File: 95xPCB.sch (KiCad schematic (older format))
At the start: 20 parts

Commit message: v1b2.7
more matrix stuff
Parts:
- removed R? (x2): 22, symbol Device:R_Small
- added R? (x2): R_Small, symbol Device:R_Small
- gave numbers to parts that had none: 18
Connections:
- net labels added: col0, col1, col10, col11, col12, col13, col14, col2, col3, col4, col7, col8, col9
- wire segments 84 -> 95
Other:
- moved on the sheet: J1

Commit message: v1b3
who knows at this point, let's be real it was kicad doing a funny
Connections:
- wire segments 95 -> 90
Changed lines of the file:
@@
 col14
 Wire Wire Line
-	4500 4000 4850 4000
-Wire Wire Line
-	4500 4100 4950 4100
-Wire Wire Line
 	4500 4200 4850 4200
-Wire Wire Line
-	4950 4100 4950 3900
-Wire Wire Line
-	4950 3900 5500 3900
-Wire Wire Line
-	5500 3900 5500 4100
-Connection ~ 4950 4100
-Wire Wire Line
-	4950 4100 5050 4100
-Wire Wire Line
-	4850 4000 4850 3850
-Wire Wire Line
-	4850 3850 5350 3850
-Wire Wire Line
-	5350 3850 5350 4000
-Connection ~ 4850 4000
-Wire Wire Line
-	4850 4000 5050 4000
 Wire Wire Line
 	4850 4200 4850 4300
@@
 Wire Wire Line
 	4850 4200 5050 4200
+Wire Wire Line
+	4500 4100 5050 4100
+Wire Wire Line
+	4500 4000 4850 4000
+Wire Wire Line
+	4850 4000 4850 3900
+Wire Wire Line
+	4850 3900 5350 3900
+Connection ~ 4850 4000
+Wire Wire Line
+	4850 4000 5050 4000
 $EndSCHEMATC

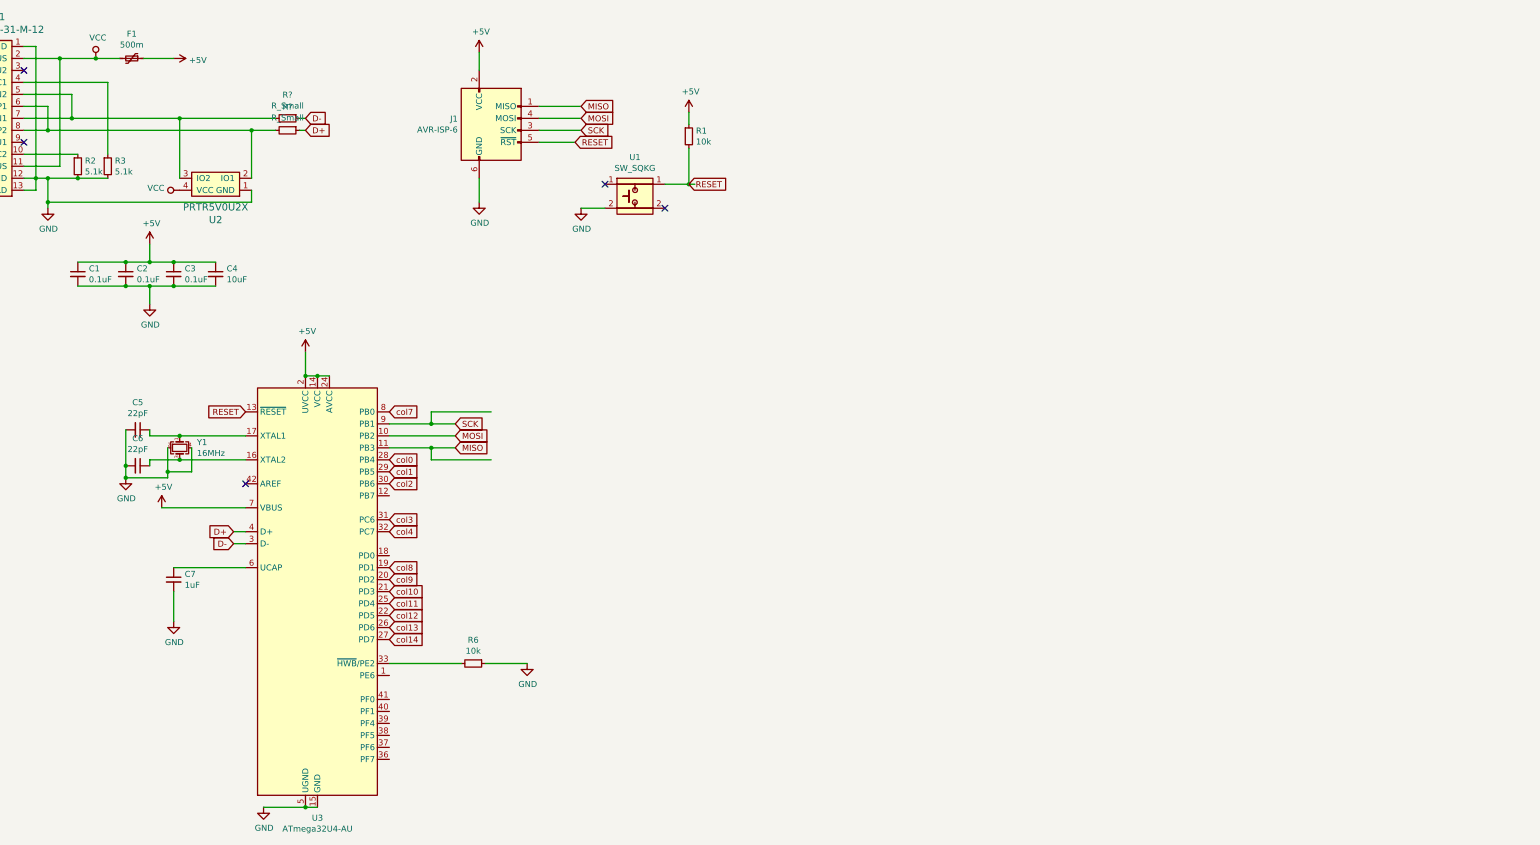
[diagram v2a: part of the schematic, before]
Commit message: v1c
Redid switch matrix for like 3rd time?
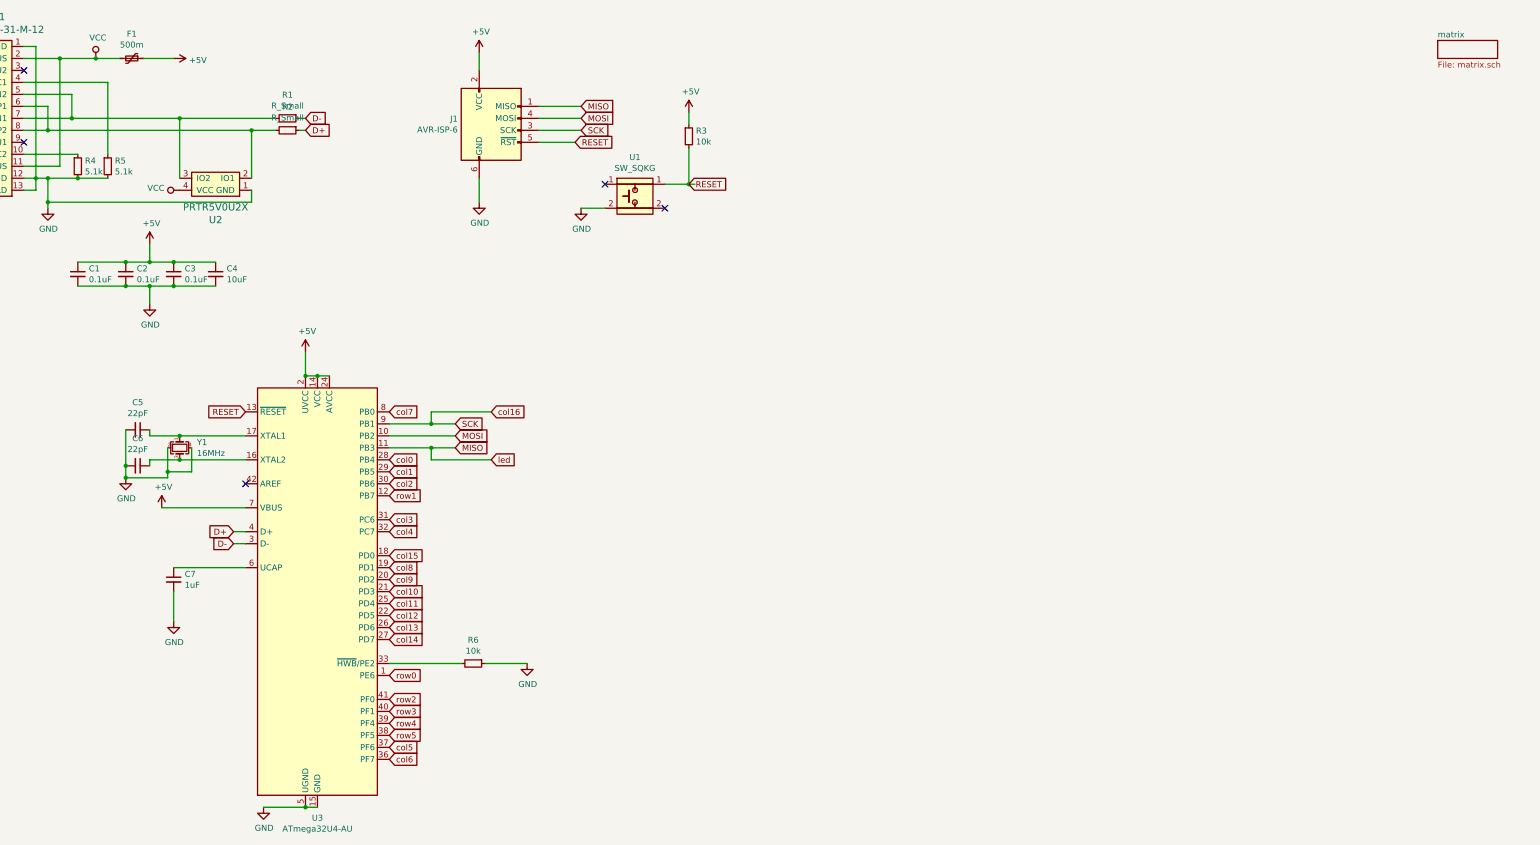
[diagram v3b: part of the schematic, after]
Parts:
- gave numbers to parts that had none: 2
- renumbered R1 to R3, R2 to R4, R3 to R5
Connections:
- net labels added: col15, col16, col5, col6, led, row0, row1, row2, row3, row4, row5
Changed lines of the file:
@@
 $Descr A4 11693 8268
 encoding utf-8
-Sheet 1 1
+Sheet 1 2
 Title ""
 Date ""
@@
 $EndDescr
 $Comp
-L power:+5V #PWR0101
+L power:+5V #PWR011
 U 1 1 63721B9F
 P 3800 3400
-F 0 "#PWR0101" H 3800 3250 50  0001 C CNN
+F 0 "#PWR011" H 3800 3250 50  0001 C CNN
 F 1 "+5V" H 3815 3573 50  0000 C CNN
 F 2 "" H 3800 3400 50  0001 C CNN
@@
 	3800 3600 3800 3400
 $Comp
-L power:GND #PWR0102
+L power:GND #PWR016
 U 1 1 63722F38
 P 3450 7200
-F 0 "#PWR0102" H 3450 6950 50  0001 C CNN
+F 0 "#PWR016" H 3450 6950 50  0001 C CNN
 F 1 "GND" H 3455 7027 50  0000 C CNN
 F 2 "" H 3450 7200 50  0001 C CNN
@@
 $EndComp
 $Comp
-L power:GND #PWR0103
+L power:GND #PWR015
 U 1 1 6372EBA5
 P 5650 6000
-F 0 "#PWR0103" H 5650 5750 50  0001 C CNN
+F 0 "#PWR015" H 5650 5750 50  0001 C CNN
 F 1 "GND" H 5655 5827 50  0000 C CNN
 F 2 "" H 5650 6000 50  0001 C CNN
@@
 	3300 5200 2700 5200
 $Comp
-L power:GND #PWR0104
+L power:GND #PWR014
 U 1 1 63737CC6
 P 2700 5650
-F 0 "#PWR0104" H 2700 5400 50  0001 C CNN
+F 0 "#PWR014" H 2700 5400 50  0001 C CNN
 F 1 "GND" H 2705 5477 50  0000 C CNN
 F 2 "" H 2700 5650 50  0001 C CNN
@@
 $EndComp
 $Comp
-L power:GND #PWR0105
+L power:GND #PWR010
 U 1 1 6373CA4C
 P 2500 3000
-F 0 "#PWR0105" H 2500 2750 50  0001 C CNN
+F 0 "#PWR010" H 2500 2750 50  0001 C CNN
 F 1 "GND" H 2505 2827 50  0000 C CNN
 F 2 "" H 2500 3000 50  0001 C CNN
@@
 $EndComp
 $Comp
-L power:+5V #PWR0106
+L power:+5V #PWR09
 U 1 1 6373DB7B
 P 2500 2500
-F 0 "#PWR0106" H 2500 2350 50  0001 C CNN
+F 0 "#PWR09" H 2500 2350 50  0001 C CNN
 F 1 "+5V" H 2515 2673 50  0000 C CNN
 F 2 "" H 2500 2500 50  0001 C CNN
@@
 	7000 1400 7000 1500
 $Comp
-L power:+5V #PWR0109
+L power:+5V #PWR04
 U 1 1 6375E019
 P 7000 1400
-F 0 "#PWR0109" H 7000 1250 50  0001 C CNN
+F 0 "#PWR04" H 7000 1250 50  0001 C CNN
 F 1 "+5V" H 7015 1573 50  0000 C CNN
 F 2 "" H 7000 1400 50  0001 C CNN
@@
 	7000 1700 7000 2000
 $Comp
-L Device:R_Small R1
+L Device:R_Small R3
 U 1 1 6375C409
 P 7000 1600
-F 0 "R1" H 7059 1646 50  0000 L CNN
+F 0 "R3" H 7059 1646 50  0000 L CNN
 F 1 "10k" H 7059 1555 50  0000 L CNN
 F 2 "" H 7000 1600 50  0001 C CNN
@@
 	6100 2200 6300 2200
 $Comp
-L power:GND #PWR0110
+L power:GND #PWR08
 U 1 1 6375A6A4
 P 6100 2200
-F 0 "#PWR0110" H 6100 1950 50  0001 C CNN
+F 0 "#PWR08" H 6100 1950 50  0001 C CNN
 F 1 "GND" H 6105 2027 50  0000 C CNN
 F 2 "" H 6100 2200 50  0001 C CNN
@@
 	5750 1550 6100 1550
 $Comp
-L power:+5V #PWR0111
+L power:+5V #PWR01
 U 1 1 637CEEF3
 P 5250 900
-F 0 "#PWR0111" H 5250 750 50  0001 C CNN
+F 0 "#PWR01" H 5250 750 50  0001 C CNN
 F 1 "+5V" H 5265 1073 50  0000 C CNN
 F 2 "" H 5250 900 50  0001 C CNN
@@
 	5250 900  5250 1050
 $Comp
-L power:GND #PWR0112
+L power:GND #PWR06
 U 1 1 637ECC94
 P 5250 2150
-F 0 "#PWR0112" H 5250 1900 50  0001 C CNN
+F 0 "#PWR06" H 5250 1900 50  0001 C CNN
 F 1 "GND" H 5255 1977 50  0000 C CNN
 F 2 "" H 5250 2150 50  0001 C CNN
@@
 NoConn ~ 6800 2200
 $Comp
-L power:VCC #PWR0116
+L power:VCC #PWR05
 U 1 1 637546F2
 P 2750 2050
-F 0 "#PWR0116" H 2750 1900 50  0001 C CNN
+F 0 "#PWR05" H 2750 1900 50  0001 C CNN
 F 1 "VCC" V 2768 2177 50  0000 L CNN
 F 2 "" H 2750 2050 50  0001 C CNN
@@
 Connection ~ 1650 1950
 $Comp
-L power:GND #PWR0115
+L power:GND #PWR07
 U 1 1 6372ADC6
 P 1650 2200
-F 0 "#PWR0115" H 1650 1950 50  0001 C CNN
+F 0 "#PWR07" H 1650 1950 50  0001 C CNN
 F 1 "GND" H 1655 2027 50  0000 C CNN
 F 2 "" H 1650 2200 50  0001 C CNN
@@
 	2150 1150 2150 1750
 $Comp
-L Device:R_Small R2
+L Device:R_Small R4
 U 1 1 6389C842
 P 1900 1850
-F 0 "R2" H 1959 1896 50  0000 L CNN
+F 0 "R4" H 1959 1896 50  0000 L CNN
 F 1 "5.1k" H 1959 1805 50  0000 L CNN
 F 2 "" H 1900 1850 50  0001 C CNN
@@
 	2150 1150 1450 1150
 $Comp
-L Device:R_Small R3
+L Device:R_Small R5
 U 1 1 6387F88A
 P 2150 1850
-F 0 "R3" H 2209 1896 50  0000 L CNN
+F 0 "R5" H 2209 1896 50  0000 L CNN
 F 1 "5.1k" H 2209 1805 50  0000 L CNN
 F 2 "" H 2150 1850 50  0001 C CNN
@@
 Connection ~ 2300 4450
 $Comp
-L power:GND #PWR0108
+L power:GND #PWR012
 U 1 1 63757699
 P 2300 4450
-F 0 "#PWR0108" H 2300 4200 50  0001 C CNN
+F 0 "#PWR012" H 2300 4200 50  0001 C CNN
 F 1 "GND" H 2305 4277 50  0000 C CNN
 F 2 "" H 2300 4450 50  0001 C CNN
@@
 $EndComp
 $Comp
-L power:+5V #PWR0107
+L power:+5V #PWR013
 U 1 1 637452E3
 P 2600 4700
-F 0 "#PWR0107" H 2600 4550 50  0001 C CNN
+F 0 "#PWR013" H 2600 4550 50  0001 C CNN
 F 1 "+5V" H 2615 4873 50  0000 C CNN
 F 2 "" H 2600 4700 50  0001 C CNN
@@
 	1750 950  1450 950
 $Comp
-L power:VCC #PWR0113
+L power:VCC #PWR02
 U 1 1 6386DE51
 P 2050 950
-F 0 "#PWR0113" H 2050 800 50  0001 C CNN
+F 0 "#PWR02" H 2050 800 50  0001 C CNN
 F 1 "VCC" H 2067 1123 50  0000 C CNN
 F 2 "" H 2050 950 50  0001 C CNN
@@
 Connection ~ 2050 950
 $Comp
-L power:+5V #PWR0114
+L power:+5V #PWR03
 U 1 1 6387940F
 P 2700 950
-F 0 "#PWR0114" H 2700 800 50  0001 C CNN
+F 0 "#PWR03" H 2700 800 50  0001 C CNN
 F 1 "+5V" V 2715 1078 50  0000 L CNN
 F 2 "" H 2700 950 50  0001 C CNN
@@
 	3200 5000 3300 5000
 $Comp
-L Device:R_Small R?
+L Device:R_Small R1
 U 1 1 63763204
 P 3650 1450
-F 0 "R?" V 3454 1450 50  0000 C CNN
+F 0 "R1" V 3454 1450 50  0000 C CNN
 F 1 "R_Small" V 3545 1450 50  0000 C CNN
 F 2 "" H 3650 1450 50  0001 C CNN
@@
 $EndComp
 $Comp
-L Device:R_Small R?
+L Device:R_Small R2
 U 1 1 6376B60F
 P 3650 1550
-F 0 "R?" V 3454 1550 50  0000 C CNN
+F 0 "R2" V 3454 1550 50  0000 C CNN
 F 1 "R_Small" V 3545 1550 50  0000 C CNN
 F 2 "" H 3650 1550 50  0001 C CNN
@@
 Text GLabel 4500 4500 2    50   Input ~ 0
 col2
-Text GLabel 4500 4800 2    50   Input ~ 0
-col3
 Text GLabel 4500 4900 2    50   Input ~ 0
 col4
@@
 Wire Wire Line
 	4850 4000 5050 4000
+Text GLabel 4500 6100 2    50   Input ~ 0
+row0
+Text GLabel 4500 6300 2    50   Input ~ 0
+row2
+Text GLabel 4500 6400 2    50   Input ~ 0
+row3
+Text GLabel 4500 6500 2    50   Input ~ 0
+row4
+Text GLabel 4500 6600 2    50   Input ~ 0
+row5
+Text GLabel 4500 6700 2    50   Input ~ 0
+col5
+Text GLabel 4500 6800 2    50   Input ~ 0
+col6
+Text GLabel 4500 4600 2    50   Input ~ 0
+row1
+Text GLabel 4500 5100 2    50   Input ~ 0
+col15
+Text GLabel 5350 3900 2    50   Input ~ 0
+col16
+Text GLabel 5350 4300 2    50   Input ~ 0
+led
+Text GLabel 4500 4800 2    50   Input ~ 0
+col3
+$Sheet
+S 13250 800  500  150
+U 63757A18
+F0 "matrix" 50
+F1 "matrix.sch" 50
+$EndSheet
 $EndSCHEMATC
